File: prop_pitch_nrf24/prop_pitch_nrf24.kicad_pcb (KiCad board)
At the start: 2 copper layers, 65 x 22 mm, 53 parts, among them J1 LOAD1, J2 LOAD2, J3 AVR-UPDI-6, J4 SERVO2, J5 SERVO1, Q1 MMSS8550, U1 ATtiny1616-M, U2 HX711, U3 TPS563208DDCR, U4 AZ1117-5.0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

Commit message: Added serial header and address jumper
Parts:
- added J6: SERIAL, Connector_PinHeader_2.54mm:PinHeader_1x04_P2.54mm_Vertical, F.Cu at (173.6, 67.5)
- added JP1: ADDRESS, Jumper:SolderJumper-3_P1.3mm_Open_Pad1.0x1.5mm_NumberLabels, F.Cu at (178.7, 67.0)
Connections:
- U1 pad 10: unconnected-(U1-PB4-Pad10) -> /ADDRESS
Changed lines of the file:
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@@
   (net 40 "unconnected-(J3-NC-Pad4)")
   (net 41 "unconnected-(J3-NC-Pad5)")
-  (net 42 "unconnected-(U1-PB4-Pad10)")
+  (net 42 "/ADDRESS")
   (net 43 "unconnected-(U2-XO-Pad13)")
   (net 44 "/RX")
@@
     )
   )
+  (footprint "Jumper:SolderJumper-3_P1.3mm_Open_Pad1.0x1.5mm_NumberLabels" (layer "F.Cu")
+    (at 178.7 67)
+    (descr "SMD Solder Jumper, 1x1.5mm Pads, 0.3mm gap, open, labeled with numbers")
+    (tags "solder jumper open")
+    (property "Sheetfile" "prop_pitch_nrf24.kicad_sch")
+    (property "Sheetname" "")
+    (property "ki_description" "Jumper, 3-pole, both open")
+    (property "ki_keywords" "Jumper SPDT")
+    (attr exclude_from_pos_files)
+    (fp_text reference "JP1" (at 0 -1.8) (layer "F.SilkS")
+        (effects (font (size 1 1) (thickness 0.15)))
+    )
+    (fp_text value "ADDRESS" (at 0 1.9) (layer "F.Fab")
+        (effects (font (size 1 1) (thickness 0.15)))
+    )
+    (fp_text user "1" (at -2.6 0) (layer "F.SilkS")
+        (effects (font (size 1 1) (thickness 0.15)))
+    )
+    (fp_text user "3" (at 2.6 0) (layer "F.SilkS")
+        (effects (font (size 1 1) (thickness 0.15)))
+    )
+    (fp_line (start -2.05 -1) (end 2.05 -1)
+      (stroke (width 0.12) (type solid)) (layer "F.SilkS"))
+    (fp_line (start -2.05 1) (end -2.05 -1)
+      (stroke (width 0.12) (type solid)) (layer "F.SilkS"))
+    (fp_line (start 2.05 -1) (end 2.05 1)
+      (stroke (width 0.12) (type solid)) (layer "F.SilkS"))
+    (fp_line (start 2.05 1) (end -2.05 1)
+      (stroke (width 0.12) (type solid)) (layer "F.SilkS"))
+    (fp_line (start -2.3 -1.25) (end -2.3 1.25)
+      (stroke (width 0.05) (type solid)) (layer "F.CrtYd"))
+    (fp_line (start -2.3 -1.25) (end 2.3 -1.25)
+      (stroke (width 0.05) (type solid)) (layer "F.CrtYd"))
+    (fp_line (start 2.3 1.25) (end -2.3 1.25)
+      (stroke (width 0.05) (type solid)) (layer "F.CrtYd"))
+    (fp_line (start 2.3 1.25) (end 2.3 -1.25)
+      (stroke (width 0.05) (type solid)) (layer "F.CrtYd"))
+    (pad "1" smd rect (at -1.3 0) (size 1 1.5) (layers "F.Cu" "F.Mask")
+      (net 3 "+5V") (pinfunction "A") (pintype "passive"))
+    (pad "2" smd rect (at 0 0) (size 1 1.5) (layers "F.Cu" "F.Mask")
+      (net 42 "/ADDRESS") (pinfunction "C") (pintype "passive"))
+    (pad "3" smd rect (at 1.3 0) (size 1 1.5) (layers "F.Cu" "F.Mask")
+      (net 2 "GND") (pinfunction "B") (pintype "passive"))
+  )
   (footprint "Capacitor_SMD:C_0805_2012Metric" (layer "F.Cu")
     (at 151 74)
@@
       (net 3 "+5V") (pinfunction "VI") (pintype "power_in"))
     (model "${KICAD6_3DMODEL_DIR}/Package_TO_SOT_SMD.3dshapes/SOT-223.wrl"
+      (offset (xyz 0 0 0))
+      (scale (xyz 1 1 1))
+      (rotate (xyz 0 0 0))
+    )
+  )
+  (footprint "Connector_PinHeader_2.54mm:PinHeader_1x04_P2.54mm_Vertical" (layer "F.Cu")
+    (at 173.55 67.55)
+    (descr "Through hole straight pin header, 1x04, 2.54mm pitch, single row")
+    (tags "Through hole pin header THT 1x04 2.54mm single row")
+    (property "Sheetfile" "prop_pitch_nrf24.kicad_sch")
+    (property "Sheetname" "")
+    (property "exclude_from_bom" "")
+    (property "ki_description" "Generic connector, single row, 01x04, script generated (kicad-library-utils/schlib/autogen/connector/)")
+    (property "ki_keywords" "connector")
+    (attr through_hole exclude_from_bom)
+    (fp_text reference "J6" (at 0 -2.33) (layer "F.SilkS")
+        (effects (font (size 1 1) (thickness 0.15)))
+    )
+    (fp_text value "SERIAL" (at 0 9.95) (layer "F.Fab")
+        (effects (font (size 1 1) (thickness 0.15)))
+    )
+    (fp_text user "${REFERENCE}" (at 0 3.81 90) (layer "F.Fab")
+        (effects (font (size 1 1) (thickness 0.15)))
+    )
+    (fp_line (start -1.33 -1.33) (end 0 -1.33)
+      (stroke (width 0.12) (type solid)) (layer "F.SilkS"))
+    (fp_line (start -1.33 0) (end -1.33 -1.33)
+      (stroke (width 0.12) (type solid)) (layer "F.SilkS"))
+    (fp_line (start -1.33 1.27) (end -1.33 8.95)
+      (stroke (width 0.12) (type solid)) (layer "F.SilkS"))
+    (fp_line (start -1.33 1.27) (end 1.33 1.27)
+      (stroke (width 0.12) (type solid)) (layer "F.SilkS"))
+    (fp_line (start -1.33 8.95) (end 1.33 8.95)
+      (stroke (width 0.12) (type solid)) (layer "F.SilkS"))
+    (fp_line (start 1.33 1.27) (end 1.33 8.95)
+      (stroke (width 0.12) (type solid)) (layer "F.SilkS"))
+    (fp_line (start -1.8 -1.8) (end -1.8 9.4)
+      (stroke (width 0.05) (type solid)) (layer "F.CrtYd"))
+    (fp_line (start -1.8 9.4) (end 1.8 9.4)
+      (stroke (width 0.05) (type solid)) (layer "F.CrtYd"))
+    (fp_line (start 1.8 -1.8) (end -1.8 -1.8)
+      (stroke (width 0.05) (type solid)) (layer "F.CrtYd"))
+    (fp_line (start 1.8 9.4) (end 1.8 -1.8)
+      (stroke (width 0.05) (type solid)) (layer "F.CrtYd"))
+    (fp_line (start -1.27 -0.635) (end -0.635 -1.27)
+      (stroke (width 0.1) (type solid)) (layer "F.Fab"))
+    (fp_line (start -1.27 8.89) (end -1.27 -0.635)
+      (stroke (width 0.1) (type solid)) (layer "F.Fab"))
+    (fp_line (start -0.635 -1.27) (end 1.27 -1.27)
+      (stroke (width 0.1) (type solid)) (layer "F.Fab"))
+    (fp_line (start 1.27 -1.27) (end 1.27 8.89)
+      (stroke (width 0.1) (type solid)) (layer "F.Fab"))
+    (fp_line (start 1.27 8.89) (end -1.27 8.89)
+      (stroke (width 0.1) (type solid)) (layer "F.Fab"))
+    (pad "1" thru_hole rect (at 0 0) (size 1.7 1.7) (drill 1) (layers "*.Cu" "*.Mask")
+      (net 2 "GND") (pinfunction "Pin_1") (pintype "passive"))
+    (pad "2" thru_hole oval (at 0 2.54) (size 1.7 1.7) (drill 1) (layers "*.Cu" "*.Mask")
+      (net 44 "/RX") (pinfunction "Pin_2") (pintype "passive"))
+    (pad "3" thru_hole oval (at 0 5.08) (size 1.7 1.7) (drill 1) (layers "*.Cu" "*.Mask")
+      (net 45 "/TX") (pinfunction "Pin_3") (pintype "passive"))
+    (pad "4" thru_hole oval (at 0 7.62) (size 1.7 1.7) (drill 1) (layers "*.Cu" "*.Mask")
+      (net 3 "+5V") (pinfunction "Pin_4") (pintype "passive"))
+    (model "${KICAD6_3DMODEL_DIR}/Connector_PinHeader_2.54mm.3dshapes/PinHeader_1x04_P2.54mm_Vertical.wrl"
       (offset (xyz 0 0 0))
       (scale (xyz 1 1 1))
@@
       (net 19 "/LED_{3}") (pinfunction "PB5") (pintype "bidirectional"))
     (pad "10" smd custom (at 0.8 1.45) (size 0.143431 0.143431) (layers "F.Cu" "F.Paste" "F.Mask")
-      (net 42 "unconnected-(U1-PB4-Pad10)") (pinfunction "PB4") (pintype "bidirectional+no_connect") (thermal_bridge_angle 45)
+      (net 42 "/ADDRESS") (pinfunction "PB4") (pintype "bidirectional") (thermal_bridge_angle 45)
       (options (clearance outline) (anchor circle))
       (primitives

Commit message: Claire's Layout
I did the layout!!!!!
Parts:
- J3: moved to B.Cu
- moved C5 107.3 mm to (82.3, 118.1), turned to 90 degrees
- moved C7 105.2 mm to (84.3, 118.1), turned to 90 degrees
- moved C8 100.6 mm to (88.9, 118.1), turned to 90 degrees
- moved JP1 100.4 mm to (91.7, 117.1), turned to 90 degrees
- moved J6 85.6 mm to (104.6, 118.4), turned to 90 degrees
- moved J3 83.4 mm to (98.0, 109.7), turned to 180 degrees
- moved U1 81.8 mm to (95.8, 117.7), turned to 90 degrees
- moved C3 79.4 mm to (99.8, 115.1), turned to 0 degrees
- moved R12 77.3 mm to (86.6, 118.2), turned to 90 degrees
- moved R9 77.3 mm to (99.9, 117.3)
- moved R8 75.1 mm to (100.1, 119.6)
- moved D3 72.1 mm to (87.4, 113.5)
- moved R3 72.0 mm to (87.4, 109.7)
- moved D2 71.5 mm to (85.0, 113.5)
- moved R2 71.4 mm to (85.0, 109.7)
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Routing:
- net +5V: track 83.9 -> 0.00 mm, vias 5 -> 0
- net +3.3VA: track 48.7 -> 0.00 mm, vias 2 -> 0
- net /SCK_{AMP}: track 34.4 -> 0.00 mm, vias 2 -> 0
- net /DOUT_{AMP}: track 33.8 -> 0.00 mm, vias 2 -> 0
- net /SERVO_{1}: track 31.0 -> 0.00 mm, vias 3 -> 0
- net /BATT_{SCALED}: track 23.2 -> 0.00 mm, vias 3 -> 0
- net /MOSI: track 23.2 -> 0.00 mm, vias 3 -> 0
- net /~{RESET}: track 22.7 -> 0.00 mm, vias 4 -> 0
- net /SERVO_{2}: track 18.7 -> 0.00 mm, vias 1 -> 0
- net /MISO: track 18.7 -> 0.00 mm, vias 1 -> 0
- net /SCK: track 14.9 -> 0.00 mm, vias 1 -> 0
- net GND: track 11.9 -> 0.00 mm, vias 2 -> 0
- net /LED_{1}: track 9.13 -> 0.00 mm, vias 1 -> 0
- net (no net): track 8.66 -> 0.00 mm
- net /VFB: track 7.60 -> 0.00 mm
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- removed copper zone on F.Cu, net +BATT
- removed copper zone on F.Cu, net /SW
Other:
- board size 65 x 22 mm -> 75.3 x 22 mm
- board text removed: "+"
- board text removed: "-"
- board text removed: "SAVO BAJIC"

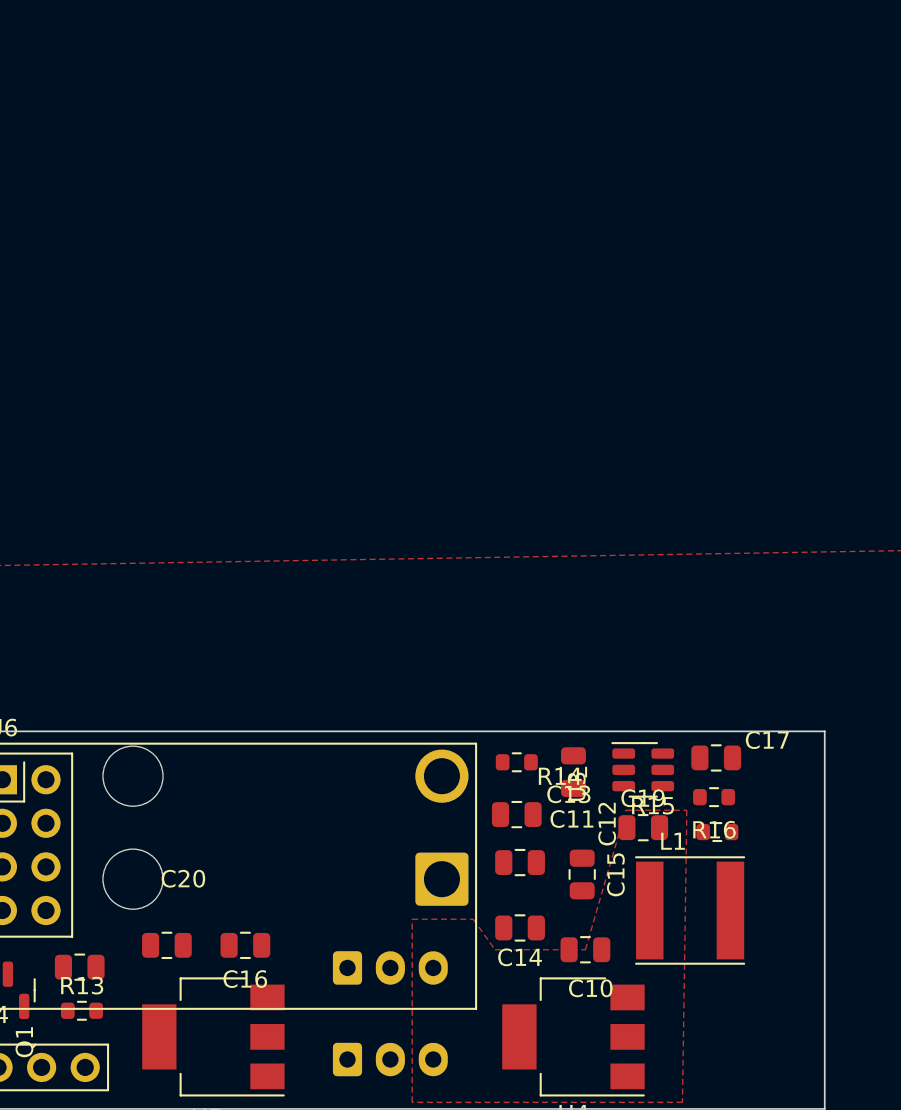
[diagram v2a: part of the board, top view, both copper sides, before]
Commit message: Revised buck circuit and added symbol
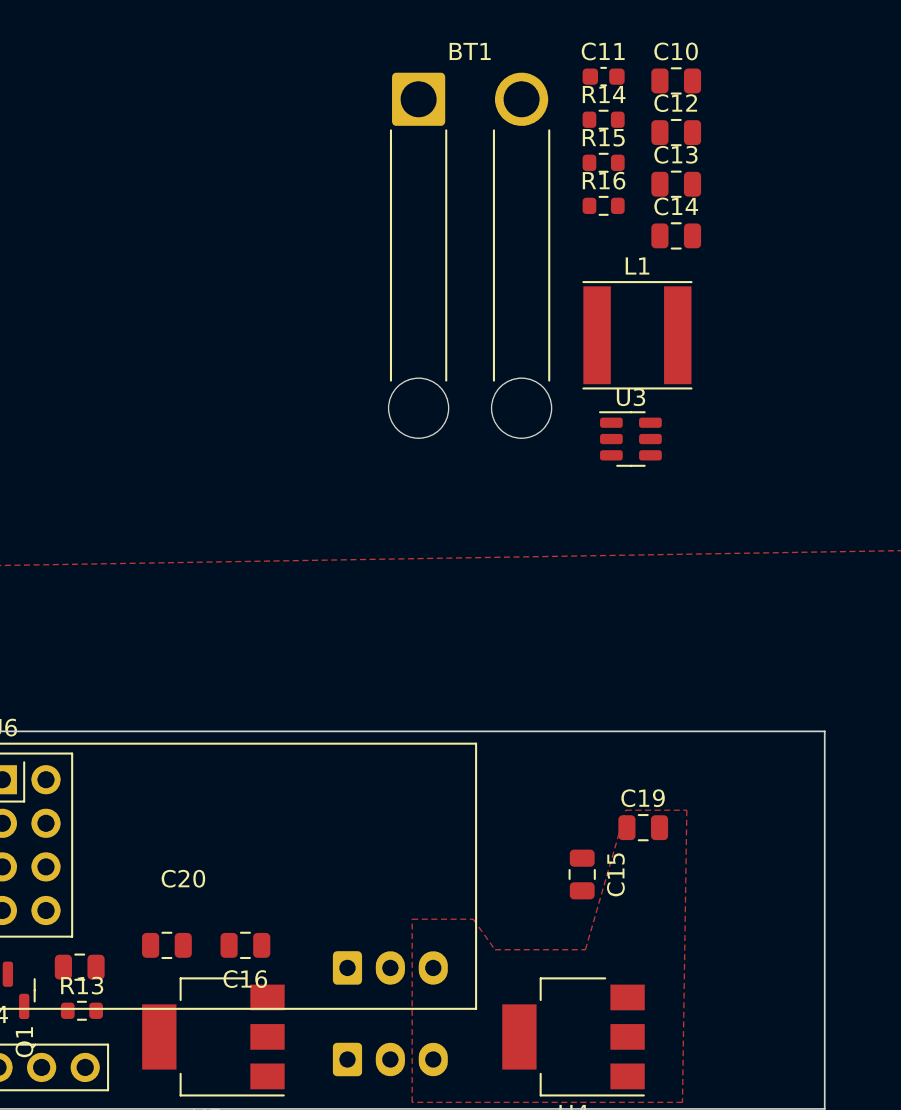
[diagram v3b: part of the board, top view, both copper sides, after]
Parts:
- removed C17: 100n, Capacitor_SMD:C_0805_2012Metric
- BT1: moved to F.Cu
- C10: value 22uF -> 10u
- C11: value 22uF -> 100n; footprint Capacitor_SMD:C_0805_2012Metric -> Capacitor_SMD:C_0603_1608Metric
- C12: value 22uF -> 100n
- C13, C14: value 22uF -> 22u
- L1: value 3.3uH -> 3u3
- R15: value 54.9k -> 54k9
- moved C10 50.9 mm to (146.7, 60.9)
- moved C11 46.0 mm to (142.5, 60.6), turned to 0 degrees
- moved BT1 45.5 mm to (131.7, 62.0), turned to 0 degrees
- moved C14 41.3 mm to (146.7, 69.9), turned to 0 degrees
- moved R15 39.6 mm to (142.5, 65.7)
- moved C13 37.9 mm to (146.7, 66.9), turned to 0 degrees
- moved R14 37.8 mm to (142.5, 63.1), turned to 0 degrees
- moved C12 37.7 mm to (146.7, 63.9), turned to 0 degrees
- moved R16 35.0 mm to (142.5, 68.2), turned to 0 degrees
- moved L1 33.7 mm to (144.4, 75.7)
- moved U3 19.3 mm to (144.1, 81.8)
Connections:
- net /VFB renamed /FB
- C10 pad 2: +5V -> +BATT
- C12 pad 1: GND -> Net-(U3-VBST)
- C12 pad 2: +5V -> Net-(U3-SW)
- C13 pad 2: +BATT -> +5V
- C14 pad 2: +BATT -> +5V
- L1 pad 1: +5V -> Net-(U3-SW)
- L1 pad 2: /SW -> +5V
- R14 pad 1: /EN -> +BATT
- R14 pad 2: +BATT -> Net-(U3-EN)
- U3 pad 2: /SW -> Net-(U3-SW)
- U3 pad 5: /EN -> Net-(U3-EN)
- U3 pad 6: /BST -> Net-(U3-VBST)

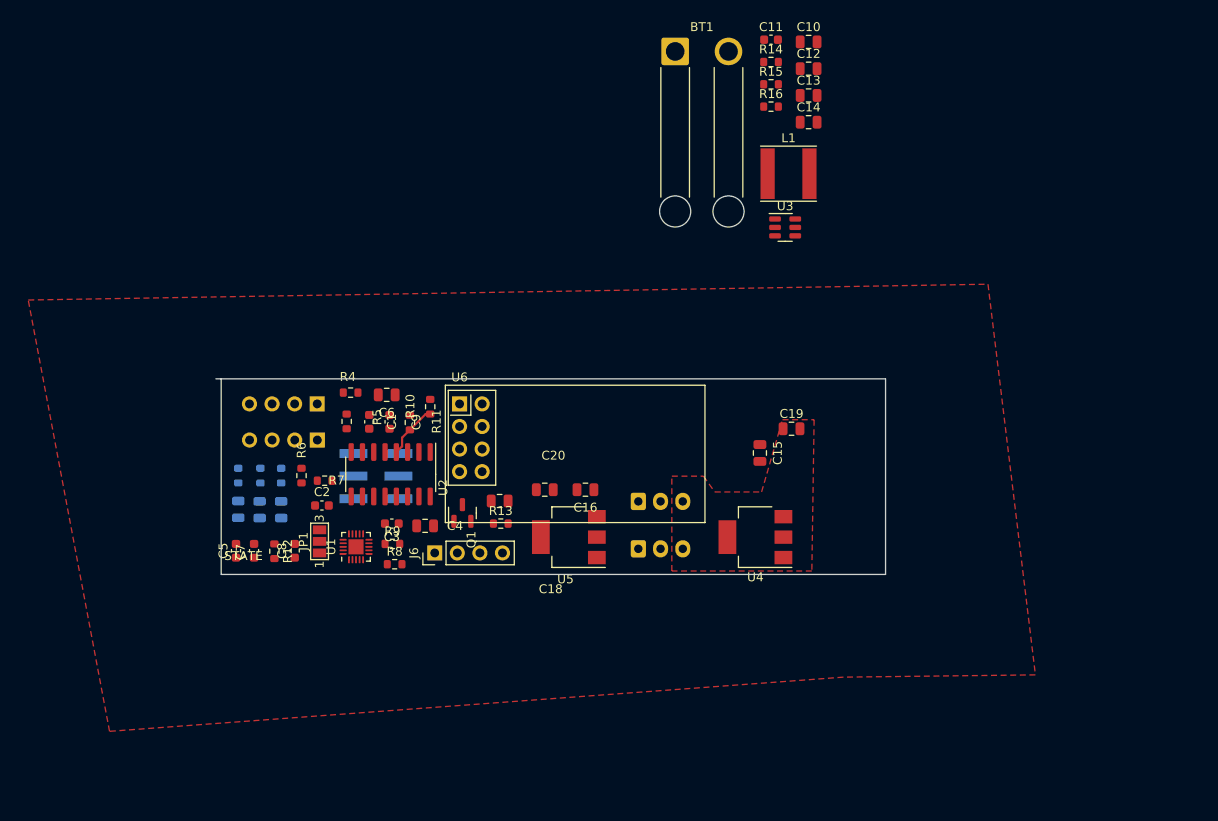
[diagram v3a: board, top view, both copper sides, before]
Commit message: Finished first version of prop control layout
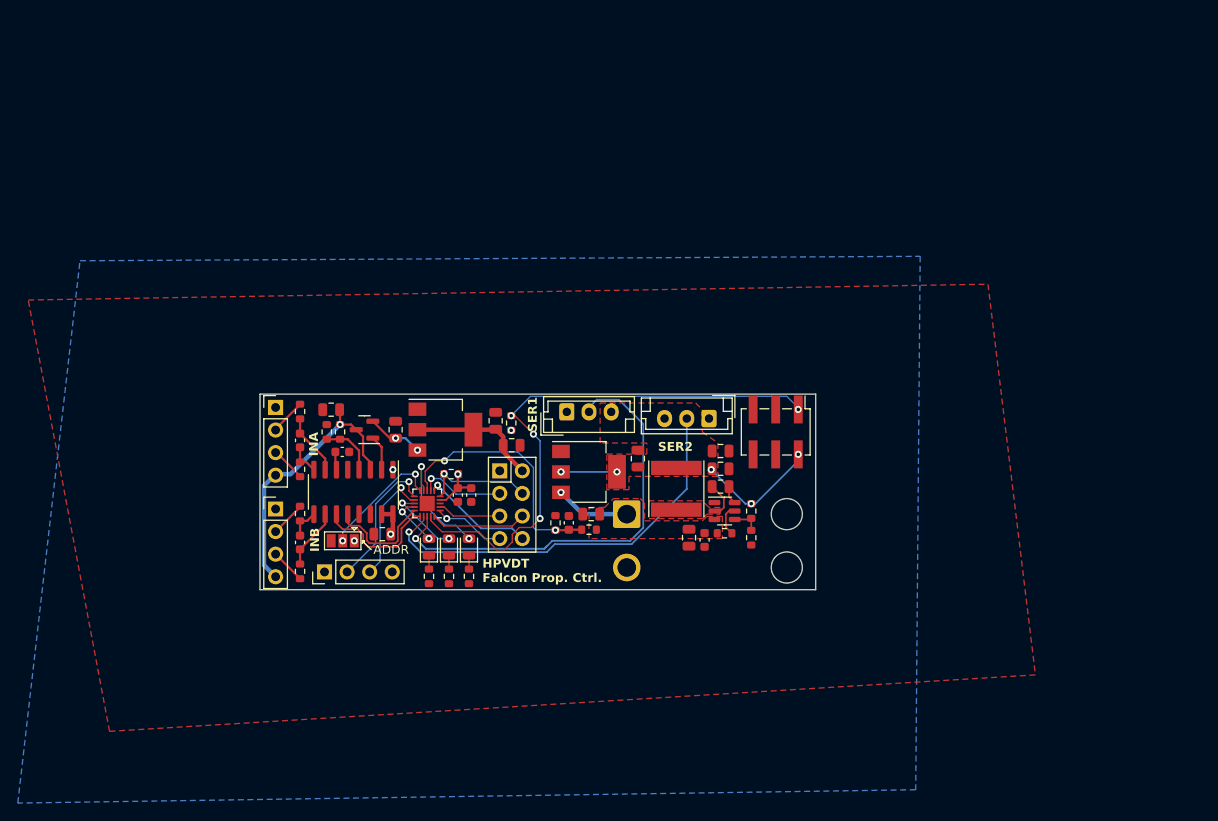
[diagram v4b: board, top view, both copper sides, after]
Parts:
- removed C8: 100n, Capacitor_SMD:C_0603_1608Metric
- BT1: moved to B.Cu
- D1, D2, D3, J1, J2, J3, J4, J5, R1, R2, R3: moved to F.Cu
- JP1: footprint Jumper:SolderJumper-3_P1.3mm_Open_Pad1.0x1.5mm_NumberLabels -> Jumper:SolderJumper-3_P1.3mm_Open_Pad1.0x1.5mm
- moved C10 57.4 mm to (133.2, 116.7), turned to 90 degrees
- moved C11 56.8 mm to (135.0, 116.9), turned to 90 degrees
- moved R14 53.3 mm to (137.2, 116.2)
- moved BT1 52.3 mm to (126.2, 114.0), turned to -90 degrees
- moved R16 48.5 mm to (140.2, 116.7), turned to 90 degrees
- moved R15 48.0 mm to (140.2, 113.7), turned to -90 degrees
- moved C12 48.0 mm to (136.8, 110.9), turned to 180 degrees
- moved J3 45.2 mm to (143.0, 104.8), turned to -90 degrees
- moved C13 41.2 mm to (136.8, 106.9), turned to 180 degrees
- moved C14 40.2 mm to (136.8, 108.9), turned to 180 degrees
- moved L1 37.6 mm to (131.8, 111.2), turned to 90 degrees
- moved U3 32.6 mm to (137.2, 113.7)
- moved R12 30.3 mm to (113.2, 103.8)
- moved C5 27.2 mm to (108.8, 111.8), turned to -90 degrees
- moved R1 24.3 mm to (104.0, 121.0), turned to -90 degrees
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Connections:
- U1 pad 17: /SERVO_{1} -> /SERVO_{2}
- U1 pad 18: /SERVO_{2} -> /SERVO_{1}
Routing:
- net /SERVO_{1}: track 0.00 -> 65.7 mm, vias 0 -> 1
- net /~{RESET}: track 0.00 -> 63.1 mm, vias 0 -> 4
- net /SERVO_{2}: track 0.00 -> 46.0 mm, vias 0 -> 1
- net +5V: track 0.00 -> 36.6 mm, vias 0 -> 12
- net +3.3VA: track 0.00 -> 31.1 mm, vias 0 -> 1
- net /BATT_{SCALED}: track 0.00 -> 28.4 mm, vias 0 -> 2
- net /RX: track 0.00 -> 15.7 mm, vias 0 -> 1
- net /SCK_{AMP}: track 0.00 -> 14.3 mm
- net +3V3: track 0.00 -> 13.9 mm
- net /ADDRESS: track 0.00 -> 13.9 mm, vias 0 -> 2
- net /LED_{3}: track 0.00 -> 13.8 mm, vias 0 -> 2
- net /TX: track 0.00 -> 13.2 mm, vias 0 -> 1
- net /INT_{nRF}: track 0.00 -> 12.8 mm, vias 0 -> 1
- net /~{CS}_{nRF}: track 0.00 -> 12.4 mm, vias 0 -> 1
- net /DOUT_{AMP}: track 0.00 -> 12.3 mm
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- added copper zone on B.Cu, net +5V
- added copper zone on F.Cu, net +BATT
- added copper zone on F.Cu, net Net-(U3-SW)
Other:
- board size 75.3 x 22 mm -> 62.5 x 22 mm
- board text added: "ADDR"
- board text added: "BATT COVERS THIS"
- board text added: "Claire N. Savo B."
- board text added: "GND COVERS THIS"
- board text added: "HPVDT Falcon Prop. Ctrl."
- board text added: "INA"
- board text added: "INB"
- board text added: "SER1"
- board text added: "SER2"
- board text added: "Wheee sensors!"
- board text removed: "EN"
- board text removed: "HPVDT Falcon Propellor Pitch & Load"
- board text removed: "STATE"
